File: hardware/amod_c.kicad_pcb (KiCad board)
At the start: 4 copper layers, 100 x 100 mm, 209 parts, among them J1001 SMA, J1002 SMA, J1003 CE, J101 USB-C, J102 rails, J1101 SMA, J1102 SMA, J1201 SMA, J1202 SMA, J201 SMA, J202 SMA, J203 SMA, J204 SMA, J301 SMA, J302 SMA, J401 SMA, J402 SMA, J501 SMA, J502 SMA, J601 SMA, J602 SMA, J603 SMA, J701 SMA, J702 SMA, J801 SMA, J802 SMA, J901 SMA, J902 SMA, J903 SMA, J904 Pmod, Q1001 AO3401A, Q1002 DMMT3904W, Q1003 MMBT3904, Q1101 AO3401A, Q1201 AO3401A, Q201 AO3401A, Q202 AO3400A, Q301 AO3401A, Q401 AO3401A, Q501 AO3401A, Q601 AO3401A, Q701 AO3401A, Q801 AO3401A, Q901 AO3401A, Q902 BCM857BS, Q903 DMMT3904W, Q904 MMBT3904, SW1001 ON, SW1101 ON, SW1201 ON, SW201 ON, SW301 ON, SW401 ON, SW501 ON, SW601 ON, SW701 ON, SW801 ON, SW901 ON, U101 LM2664, U102 3.3V, U1101 TLC555, U1201 OPA2197, U201 TLV62568, U202 TPS7A2033, U203 OPA810, U301 LV1T34, U302 ICL7660A, U401 MAX7410, U402 LV1T34, U501 TMUX4053, U502 OPA810, U601 OPA2810, U602 TLV3501, U603 74LVC1G79, U604 74LVC1G3157, U605 74LVC1G3157, U701 LF398, U801 TLV3201, U901 OPA810

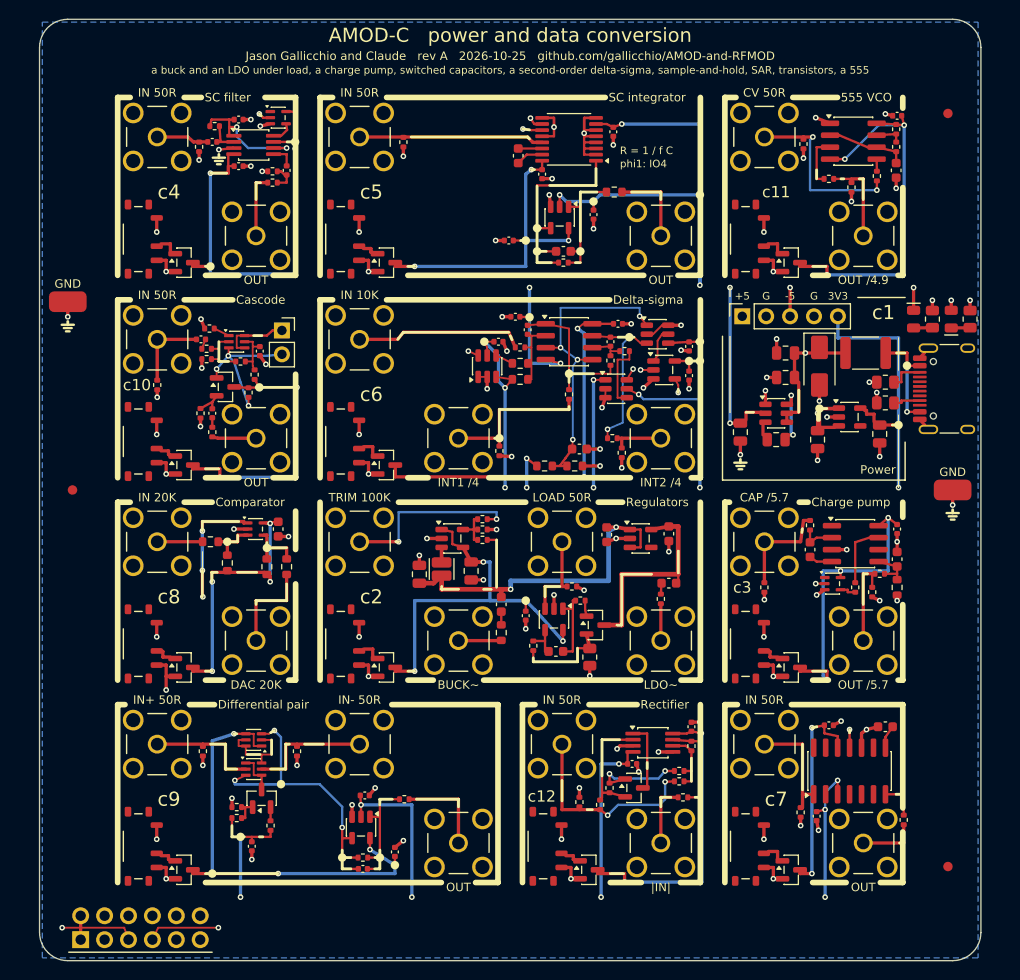
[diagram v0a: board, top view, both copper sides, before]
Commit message: AMOD-C: DRC 0 (Prompt 19). The Pmod's eight lines in lanes that never cross (the IOs reassigned so they nest: c5 IO8/IO4, c4 IO3, c8 IO2 down the left margin; c6 IO1/IO7, c7 IO5, c3 IO6 along the bottom); c6's bit and clock routed to its corner; the scope ground loops in the right margin
Co-Authored-By: Claude Opus 5.5 <noreply@anthropic.com>
Claude-Session: https://claude.ai/code/session_01RKeoKvFFzjk3cEBLCXXHnB
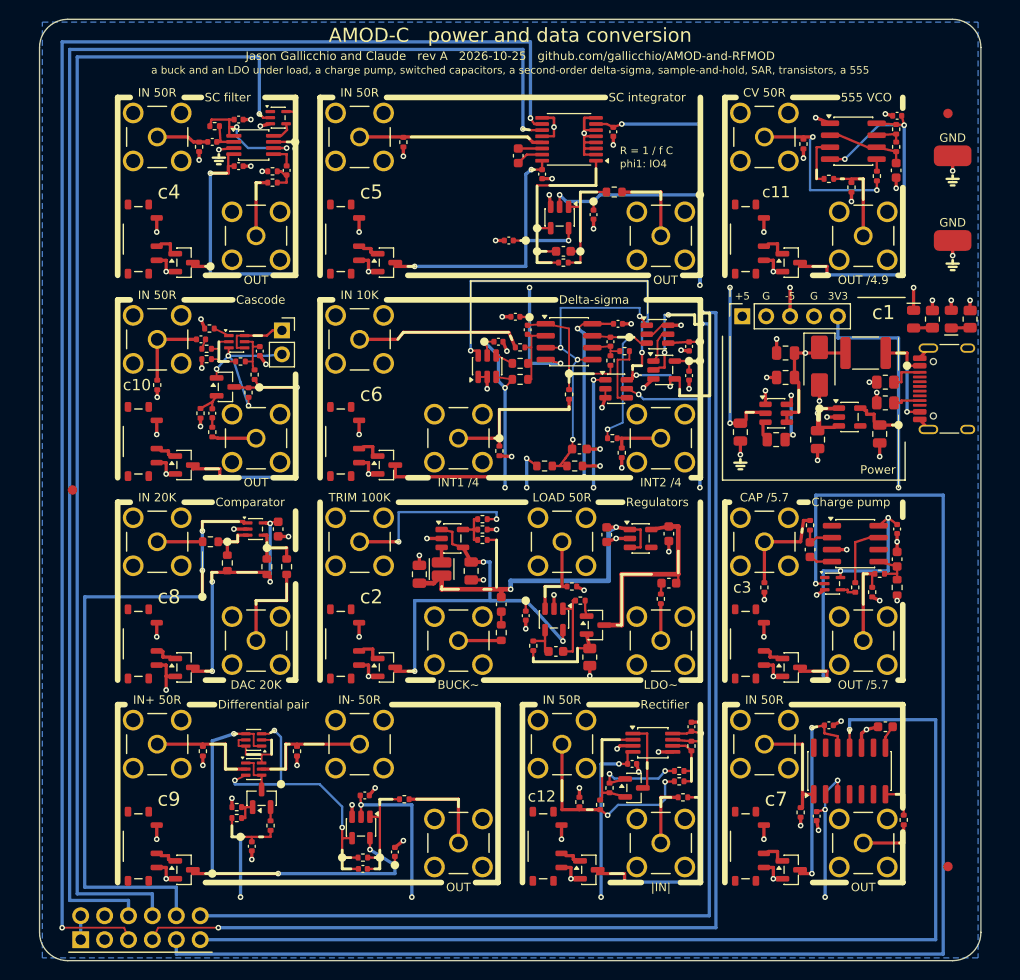
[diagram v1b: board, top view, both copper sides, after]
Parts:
- moved TP9901 95.3 mm to (97.0, 14.5)
- moved TP9902 26.5 mm to (97.0, 23.5)
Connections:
- U301 pad 2: /PMOD7 -> /PMOD6
- U603 pad 2: /PMOD5 -> /PMOD1
- U603 pad 4: /PMOD6 -> /PMOD7
- U604 pad 6: /PMOD6 -> /PMOD7
- U605 pad 6: /PMOD6 -> /PMOD7
- U701 pad 11: /PMOD1 -> /PMOD5
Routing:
- net /PMOD7: track 8.77 -> 186.9 mm, vias 2 -> 6
- net /PMOD4: track 2.05 -> 156.9 mm
- net /PMOD8: track 9.53 -> 161.5 mm
- net /PMOD6: track 4.02 -> 155.7 mm, vias 3 -> 1
- net /PMOD1: track 1.92 -> 129.0 mm, vias 1 -> 3
- net /PMOD3: track 1.33 -> 125.9 mm
- net /PMOD5: track 1.36 -> 113.6 mm
- net /PMOD2: track 12.6 -> 68.8 mm

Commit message: AMOD-C: back panels for every tile (the front's four orphan notes moved there), a 5th-order Butterworth under c4 and the pair's tanh under c9
Co-Authored-By: Claude Opus 5.5 <noreply@anthropic.com>
Claude-Session: https://claude.ai/code/session_01RKeoKvFFzjk3cEBLCXXHnB
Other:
- board text added: "+0.2V"
- board text added: "+1 to -1 V"
- board text added: "+3.3 V 300 mA"
- board text added: "+5 V 1.5 A"
- board text added: "-0.2V"
- board text added: "-5 V 40 mA"
- board text added: "0 to -60 dB"
- board text added: "1 V max"
- board text added: "100k"
- board text added: "1k"
- board text added: "BIT on IO2"
- board text added: "C = 1 nF"
- board text added: "CLK IO1, BIT IO7"
- board text added: "CLK on IO3"
- board text added: "CV +-1 V"
- board text added: "DC to 100 kHz"
- board text added: "IN +-1 V"
- board text added: "IN +-1.65 V"
- board text added: "IN +-50 mV"
- board text added: "IN+, IN- +-0.2 V"
- board text added: "INT1, INT2 / 4"
- board text added: "IO4, IO8"
- board text added: "IO5 high: track"
- board text added: "IO5 low: hold"
- board text added: "IO6 clocks it"
- board text added: "LDO 3.3 V"
- board text added: "LOAD 100 mA/V,"
- board text added: "OUT +-1 V"
- board text added: "OUT 6.9 kHz"
- board text added: "OUT = |IN|"
- board text added: "OUT about -5 V"
- board text added: "SAR in gateware"
- board text added: "TRIM +-2 V"
- board text added: "Track/hold"
- board text added: "USB-C 5 V only"
- board text added: "buck 3.6 V 1.5 MHz"
- board text added: "c1 Power"
- board text added: "c10 Cascode"
- board text added: "c11 555 VCO"
- board text added: "c12 Rectifier"
- board text added: "c2 Regulators"
- board text added: "c3 Charge pump"
- board text added: "c4 SC filter"
- board text added: "c5 SC integrator"
- board text added: "c6 Delta-sigma"
- board text added: "c7 Track/hold"
- board text added: "c8 Comparator"
- board text added: "c9 Differential pair"
- board text added: "droop 30 mV/s"
- board text added: "fc = fCLK / 100"
- board text added: "high: IN > DAC"
- board text added: "jumper on: CE"
- board text added: "linear +-25 mV"
- board text added: "moves it"
- board text added: "needs gateware"
- board text added: "off: cascode"
- board text added: "phases IO4, IO8"
- board text added: "to 15 kHz"
- board text removed: "phi1: IO4"

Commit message: Two pinouts read against their datasheets and fixed: the DMMT3904W (AMOD-C's c9 and c10) is 1 B2, 2 B1, 3 C1, 4 E1, 5 E2, 6 C2, not the BCM857BS's order (c9's pair turned 180 with IN+ under it on the back, c10's turned 180 with Q1's base on the back); RF-MOD's 915 MHz SAW has its output on pad 4, not 3 (r4 took it from a ground pad). scripts/check_pinouts.py compares every symbol's pin names with EasyEDA's: these two were its only real disagreements
Co-Authored-By: Claude Opus 5.5 <noreply@anthropic.com>
Claude-Session: https://claude.ai/code/session_01RKeoKvFFzjk3cEBLCXXHnB
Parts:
- moved C1002 0.45 mm to (23.4, 35.7)
- turned Q1002 to 180 degrees
- turned Q903 to 180 degrees
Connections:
- Q1002 pad 1: /c10_E1 -> /c10_CB
- Q1002 pad 3: /c10_CN -> /c10_C1
- Q1002 pad 4: /c10_C1 -> /c10_E1
- Q1002 pad 5: /c10_CB -> /c10_C1
- Q1002 pad 6: /c10_C1 -> /c10_CN
- Q903 pad 1: /c9_EM -> /c9_INN
- Q903 pad 3: /c9_MO -> /c9_MD
- Q903 pad 5: /c9_INN -> /c9_EM
- Q903 pad 6: /c9_MD -> /c9_MO
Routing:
- net /c9_INP: track 12.3 -> 16.5 mm, vias 0 -> 2
- net /c10_B1: track 6.53 -> 10.3 mm, vias 0 -> 2
- net /c10_CB: track 5.44 -> 4.79 mm
- net /c10_C1: track 7.15 -> 6.50 mm
- net /c9_INN: track 13.3 -> 14.0 mm

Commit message: AMOD-C: c6's second integrator 680 pF (half the swing, the same bits: the comparator sees only its sign) and 10 k into the comparator's +IN, so the 3.3 V comparator survives an integrator at a rail; c2's LOAD reaches its op amp (whose negative rail is ground) through 1 k. Simulated: c6's second output stays inside 0-3.3 V up to 1.5 V in
Co-Authored-By: Claude Opus 5.5 <noreply@anthropic.com>
Claude-Session: https://claude.ai/code/session_01RKeoKvFFzjk3cEBLCXXHnB
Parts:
- added R210: 10R, Resistor_SMD:R_0805_2012Metric, F.Cu at (58.5, 67.8)
- added R612: 1k, Resistor_SMD:R_0402_1005Metric, F.Cu at (61.9, 46.0)
- C603: value 330p -> 680p
- R208: value 100R -> 1k
- R209: value 10R -> 100R; footprint Resistor_SMD:R_0805_2012Metric -> Resistor_SMD:R_0402_1005Metric
- R608: footprint Resistor_SMD:R_0603_1608Metric -> Resistor_SMD:R_0402_1005Metric
- R610: value 3.3k -> 10k; footprint Resistor_SMD:R_0402_1005Metric -> Resistor_SMD:R_0603_1608Metric
- R611: value 1k -> 3.3k
- moved R608 16.1 mm to (62.1, 33.8)
- moved R208 6.93 mm to (52.5, 66.5), turned to 90 degrees
- moved R209 6.08 mm to (57.5, 61.8), turned to 0 degrees
- moved R207 5.95 mm to (53.7, 60.7), turned to -90 degrees
- moved R610 4.97 mm to (56.9, 47.5)
- moved R609 3.20 mm to (53.6, 47.5)
- moved R611 1.84 mm to (60.9, 44.5), turned to 0 degrees
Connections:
- R207 pad 1: /c2_SH -> /c2_LOAD
- R207 pad 2: /c2_FBK -> /c2_LIN
- R208 pad 1: /c2_OG -> /c2_SH
- R208 pad 2: /c2_GATE -> /c2_FBK
- R209 pad 1: GND -> /c2_OG
- R209 pad 2: /c2_SH -> /c2_GATE
- R608 pad 1: +3V3 -> /c6_I2
- R608 pad 2: /c6_VM -> /c6_I2C
- R609 pad 1: /c6_VM -> +3V3
- R609 pad 2: GND -> /c6_VM
- R610 pad 1: /c6_I2 -> /c6_VM
- R610 pad 2: /c6_I2J -> GND
- R611 pad 1: GND -> /c6_I2
- U203 pad 3: /c2_LOAD -> /c2_LIN
- U602 pad 3: /c6_I2 -> /c6_I2C
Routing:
- net /PMOD7: track 186.9 -> 178.5 mm, vias 6 -> 8
- net /c2_LOAD: track 9.45 -> 7.12 mm
- net /c6_I2C: track 0.00 -> 2.17 mm
- net /c2_LIN: track 0.00 -> 1.37 mm
- net /c6_I2: track 18.1 -> 16.9 mm
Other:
- board text added: "IN +-1.5 V max"
- board text removed: "IN +-1.65 V"
